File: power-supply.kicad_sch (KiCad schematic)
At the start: 16 parts, among them U1 LT3045EMSE_PBF_5.5V, U2 ADP150AUJZ-3.3-R7, U3 ADP150AUJZ-3.0-R7, U4 ADP150AUJZ-1.8-R7

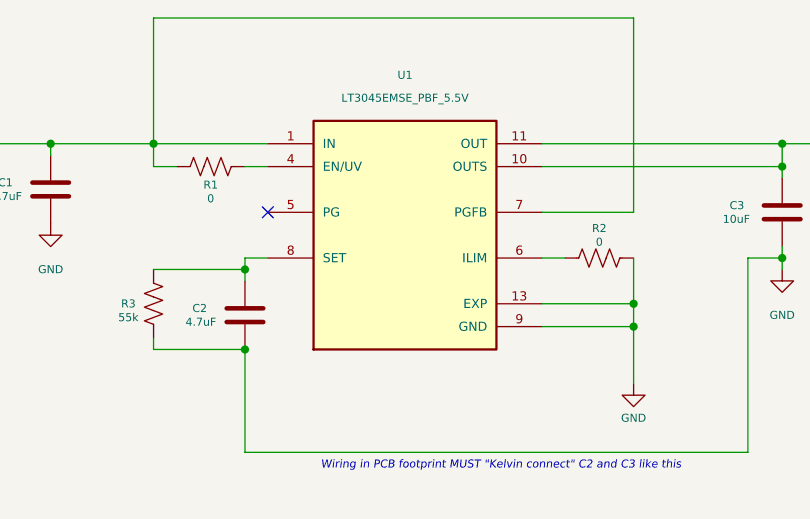
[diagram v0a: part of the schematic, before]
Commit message: Complete Schematic of the PCB
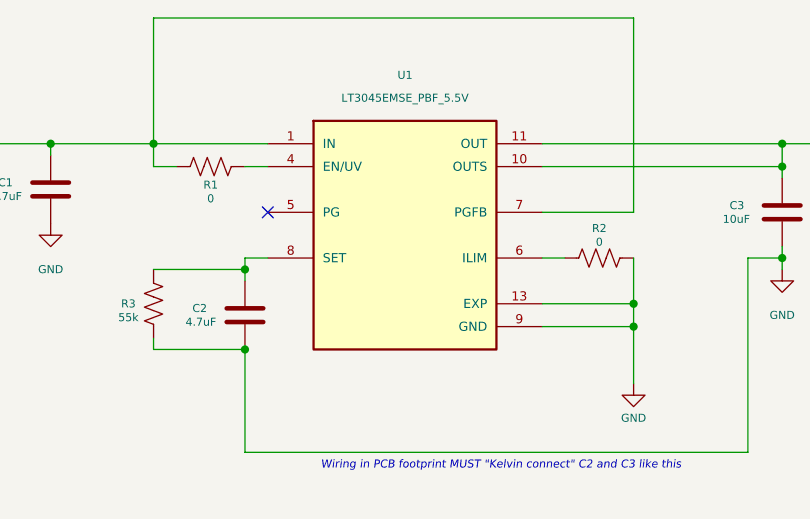
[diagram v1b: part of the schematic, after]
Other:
- title: Power Supply Module for the whole PLL system -> Power Supply Module for the PLL system
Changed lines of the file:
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@@
 	(paper "A4")
 	(title_block
-		(title "Power Supply Module for the whole PLL system")
+		(title "Power Supply Module for the PLL system")
 		(date "2026-08-31")
 		(rev "1")

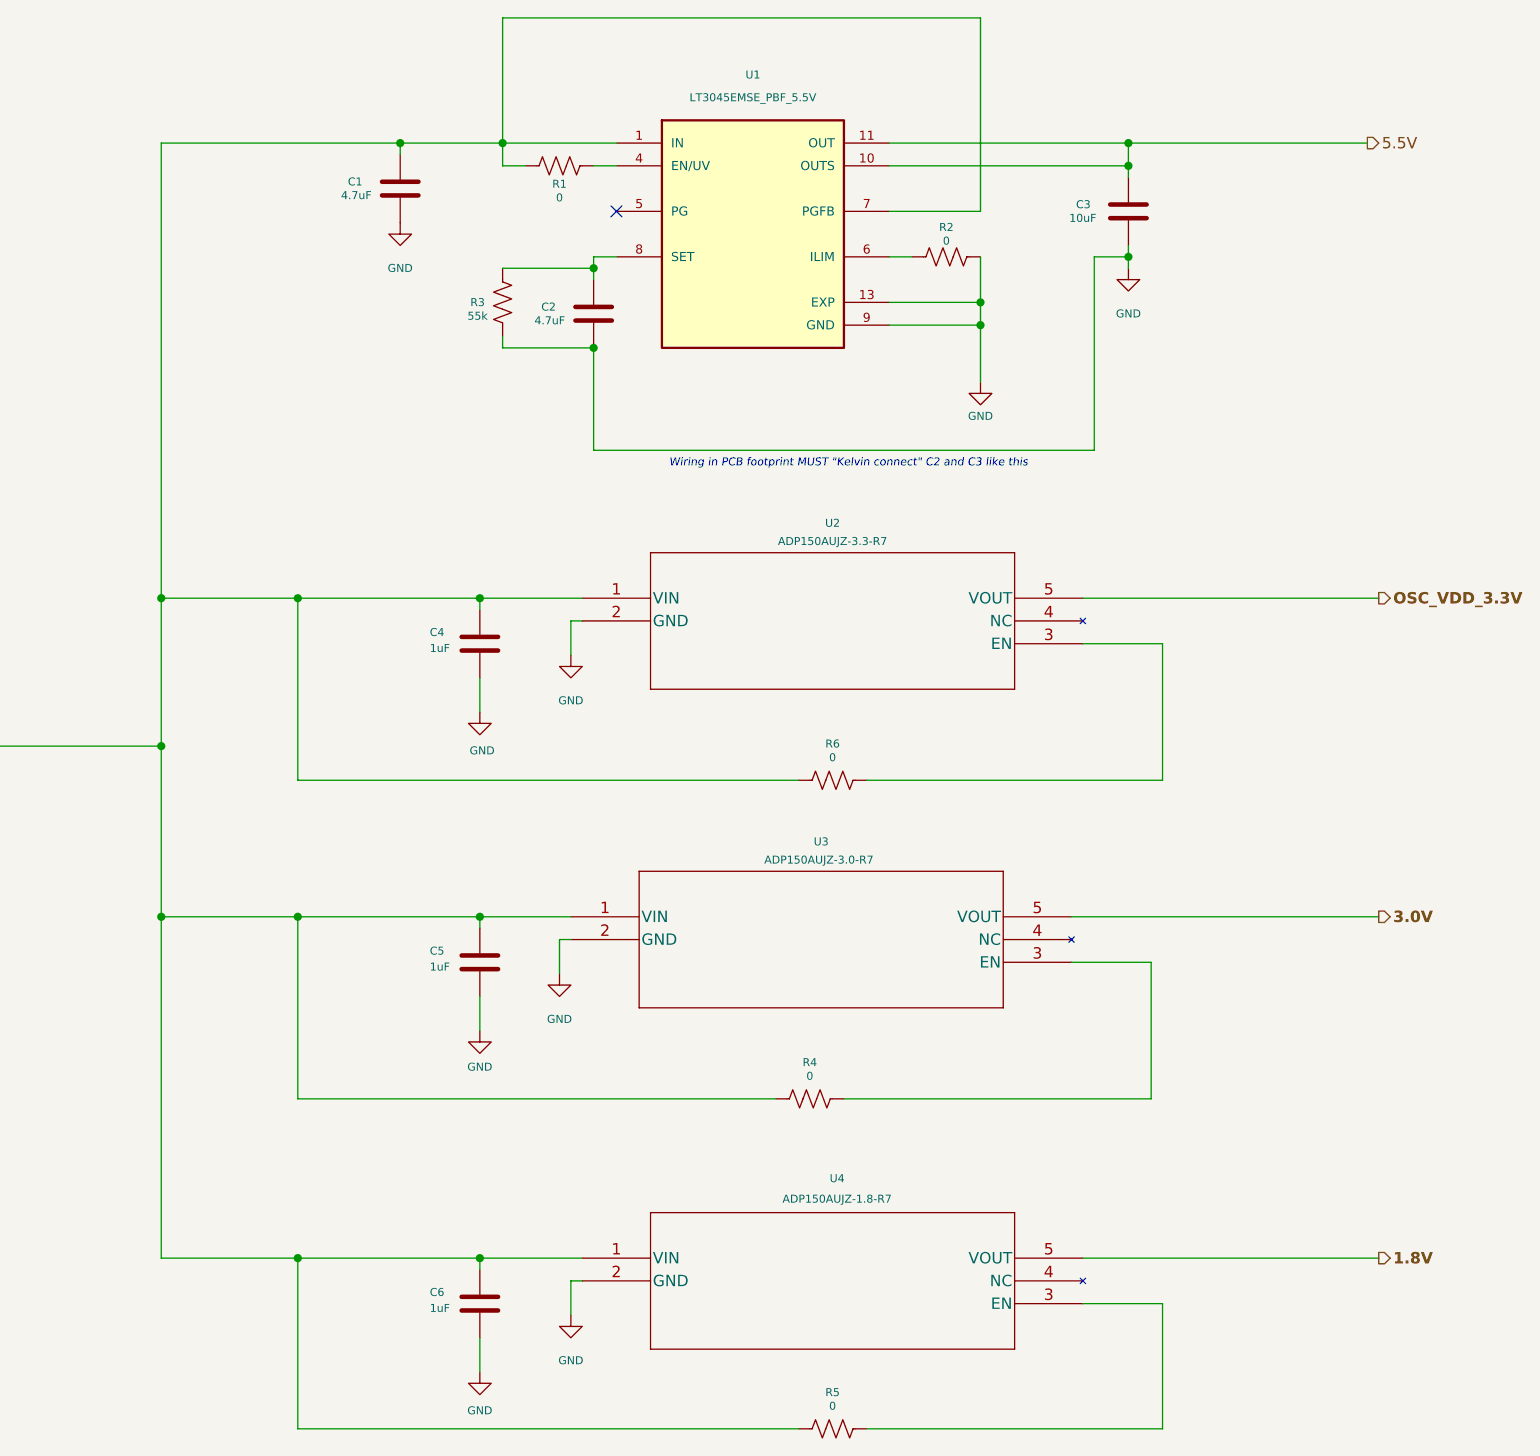
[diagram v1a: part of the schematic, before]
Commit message: Remove 0ohm resistors for EN pins and SMA connector for external REFIN
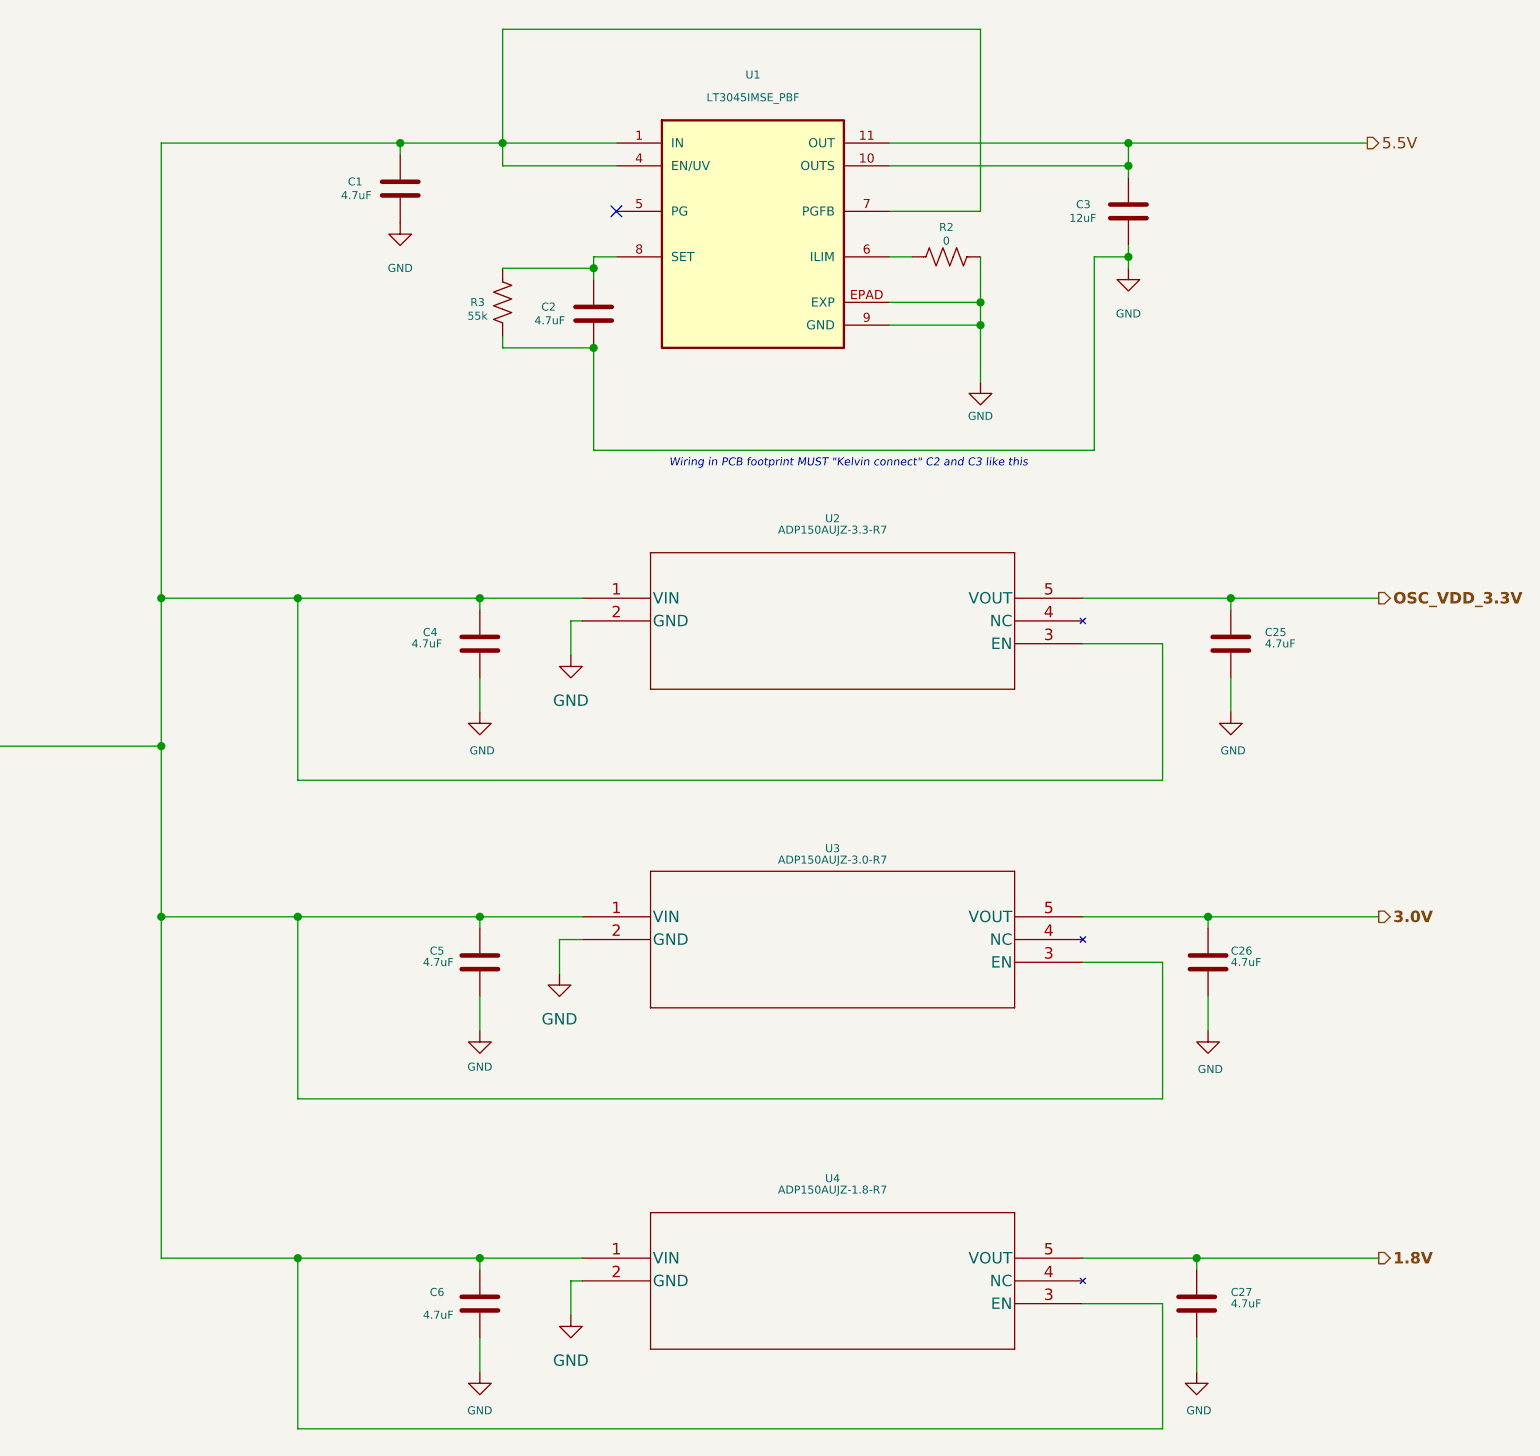
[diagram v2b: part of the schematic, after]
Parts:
- removed R1: 0, Capacitor_SMD:C_0603_1608Metric, symbol Device:R_US
- removed R4, R5, R6: 0, symbol Device:R_US
- removed U1: LT3045EMSE_PBF_5.5V, LT3045EMSE_PBF:SOP65P490X110-13N, symbol LT3045EMSE_PBF:LT3045EMSE_PBF
- removed U2: ADP150AUJZ-3.3-R7, ADP150AUJZ_3.3V_5_leads:UJ_5_ADI-M, symbol ADP150AUJZ_3.3V_5_leads:ADP150AUJZ-3.3-R7
- removed U3: ADP150AUJZ-3.0-R7, ADP150AUJZ_3.0V_5_leads:UJ_5_ADI-M, symbol ADP150AUJZ_5_leads:ADP150AUJZ-3.0-R7
- added C25, C26, C27: 4.7uF, Capacitor_SMD:C_0402_1005Metric, symbol Device:C
- added U1: LT3045IMSE_PBF, LT3045EMSE-5V5:MSOP12_MSE_ADI-L, symbol LT3045IMSE_PBF:LT3045IMSE_PBF
- added U2: ADP150AUJZ-3.3-R7, ADP150-3V3:UJ_5_ADI-L, symbol ADP150AUJZ_3.3_5_leads:ADP150AUJZ-3.3-R7
- added U3: ADP150AUJZ-3.0-R7, ADP150-3V:UJ_5_ADI-L, symbol ADP150AUJZ_3.0V_5_leads:ADP150AUJZ-3.0-R7
- C1, C2, R2, R3: footprint Capacitor_SMD:C_0603_1608Metric -> Capacitor_SMD:C_0402_1005Metric
- C3: value 10uF -> 12uF; footprint Capacitor_SMD:C_0603_1608Metric -> Capacitor_SMD:C_1206_3216Metric
- C4, C5, C6: value 1uF -> 4.7uF
- U4: footprint ADP150AUJZ_1.8V_5_leads:UJ_5_ADI-M -> ADP150-1V8:UJ_5_ADI-L
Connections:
- net +6.5V_RAW: now also U4.3 (EN), U1.1 (IN), U1.2 (IN), U1.3 (IN), U1.4 (EN/UV), U1.7 (PGFB), U2.1 (VIN), U2.3 (EN), U3.1 (VIN), U3.3 (EN)
- net 1.8V: now also C27.1
- net 3.0V: now also C26.1, U3.5 (VOUT)
- net 5.5V: now also U1.10 (OUTS), U1.11 (OUT), U1.12 (OUT)
- net GND: now also C25.2, C26.2, C27.2, U1.9 (GND), U1.EPAD (EXP), U2.2 (GND), U3.2 (GND)
- net OSC_VDD_3.3V: now also C25.1, U2.5 (VOUT)
- net at C2.1, R3.1: now also U1.8 (SET)
- net at R2.2: now also U1.6 (ILIM)

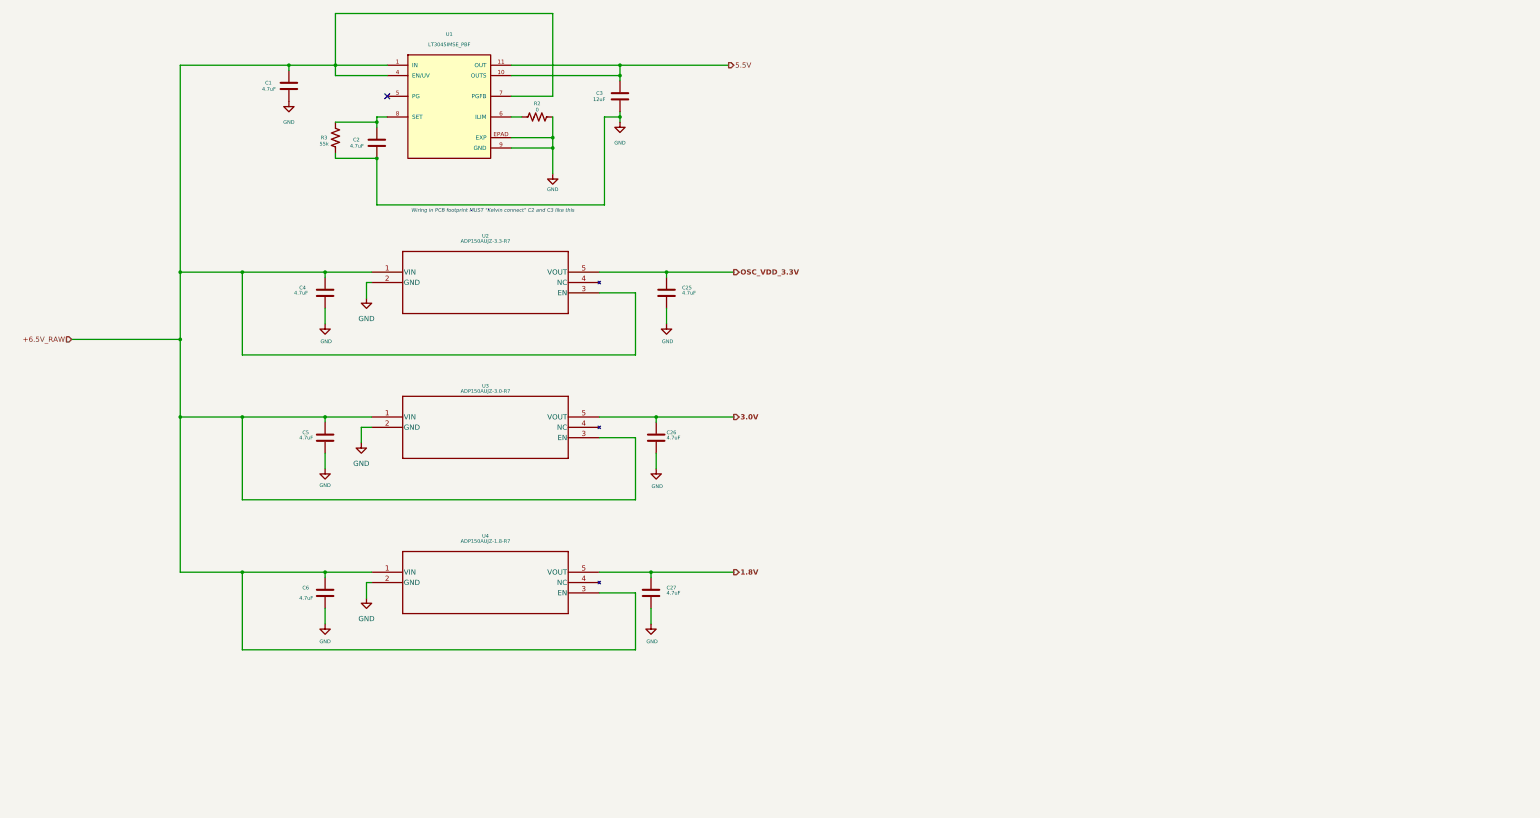
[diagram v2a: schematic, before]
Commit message: Complete and adjust the PCB based on advisor's advice and manufacturer in-stock parts
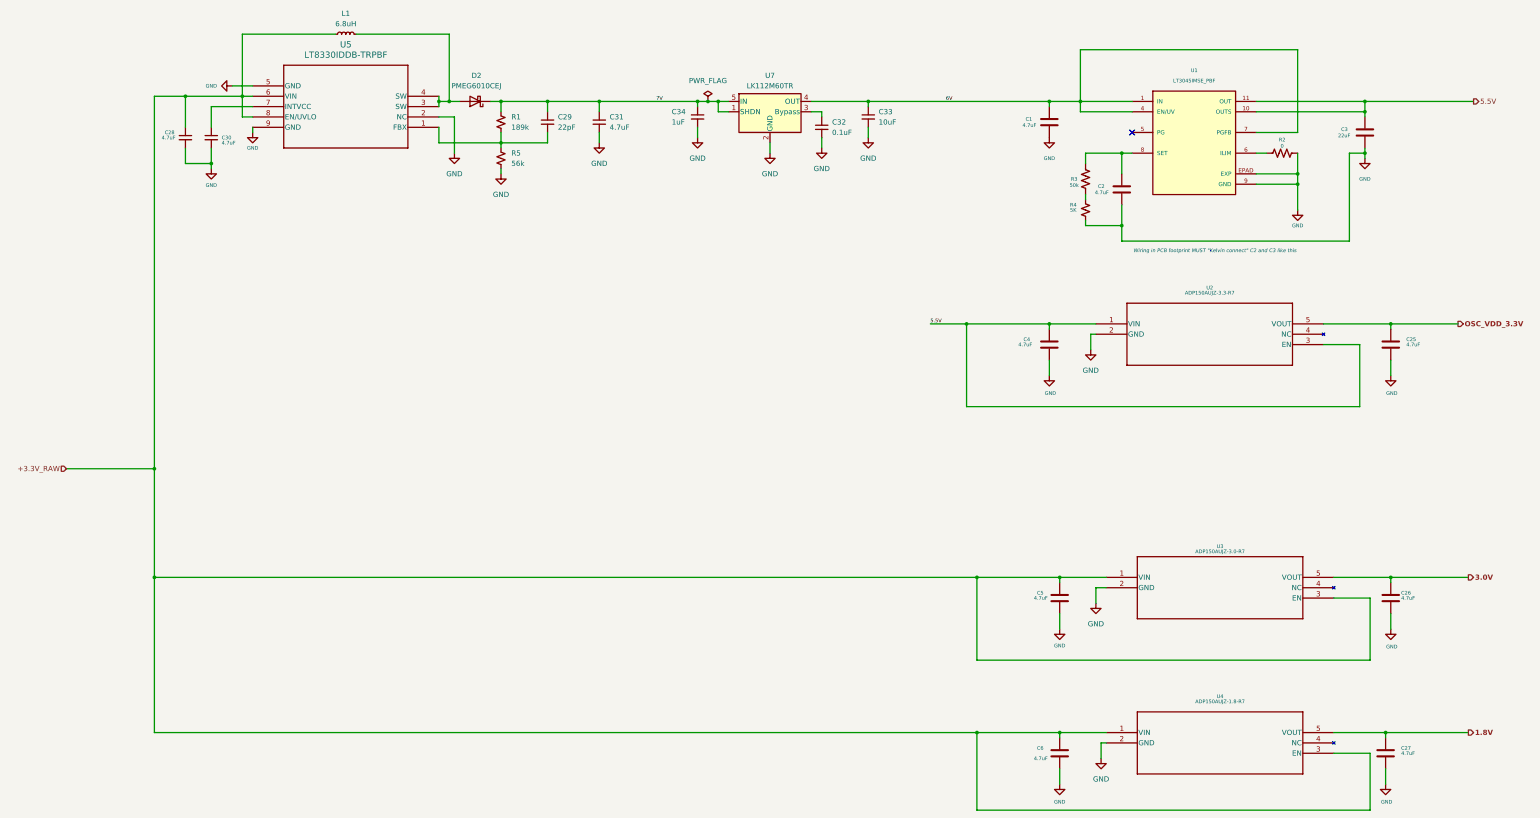
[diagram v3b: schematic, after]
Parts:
- added C28, C30, C31: 4.7uF, Capacitor_SMD:C_0402_1005Metric, symbol Device:C_Small
- added C29: 22pF, Capacitor_SMD:C_0402_1005Metric, symbol Device:C_Small
- added C32: 0.1uF, Capacitor_SMD:C_0402_1005Metric, symbol Device:C_Small
- added C33: 10uF, Capacitor_SMD:C_0603_1608Metric, symbol Device:C_Small
- added C34: 1uF, Capacitor_SMD:C_0402_1005Metric, symbol Device:C_Small
- added D2: PMEG6010CEJ, Diode_SMD:D_SOD-323F, symbol Diode:PMEG6010CEJ
- added L1: 6.8uH, Inductor_SMD:L_0603_1608Metric, symbol Device:L_Small
- added R1: 189k, Resistor_SMD:R_0603_1608Metric, symbol Device:R_Small_US
- added R4: 5K, Resistor_SMD:R_0402_1005Metric, symbol Device:R_Small_US
- added R5: 56k, Resistor_SMD:R_0805_2012Metric, symbol Device:R_Small_US
- added U5: LT8330IDDB-TRPBF, symbols:DDB_05-08-1702_ADI-L, symbol LT8330IDDB:LT8330IDDB-TRPBF
- added U7: LK112M60TR, Package_TO_SOT_SMD:SOT-23-5, symbol Regulator_Linear:LK112M60TR
- C3: value 12uF -> 22uF; footprint Capacitor_SMD:C_1206_3216Metric -> Capacitor_SMD:C_0603_1608Metric
- R2: footprint Capacitor_SMD:C_0402_1005Metric -> Resistor_SMD:R_0402_1005Metric
- R3: value 55k -> 50k; footprint Capacitor_SMD:C_0402_1005Metric -> Resistor_SMD:R_0402_1005Metric
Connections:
- net 5.5V: now also C4.1, U2.1 (VIN), U2.3 (EN)
- net GND: now also C28.2, C30.2, C31.2, C32.2, C33.2, C34.2, R4.2, R5.1, U5.2 (NC), U5.5 (GND), U5.9 (GND), U7.2 (GND); no longer R3.2
- removed net +6.5V_RAW: C1.1, C4.1, C5.1, C6.1, U1.1 (IN), U1.2 (IN), U1.3 (IN), U1.4 (EN/UV), U1.7 (PGFB), U2.1 (VIN), U2.3 (EN), U3.1 (VIN), U3.3 (EN), U4.1 (VIN), U4.3 (EN)
- new net: C29.2, R1.1, R5.2, U5.1 (FBX)
- new net: D2.2 (A), L1.2, U5.3 (SW), U5.4 (SW)
- new net: C30.1, U5.7 (INTVCC)
- new net: C32.1, U7.3 (Bypass)
- new net: R3.2, R4.1
- new net +3.3V_RAW: C28.1, C5.1, C6.1, L1.1, U3.1 (VIN), U3.3 (EN), U4.1 (VIN), U4.3 (EN), U5.6 (VIN), U5.8 (EN/UVLO)
- new net 6V: C1.1, C33.1, U1.1 (IN), U1.2 (IN), U1.3 (IN), U1.4 (EN/UV), U1.7 (PGFB), U7.4 (OUT)
- new net 7V: C29.1, C31.1, C34.1, D2.1 (K), R1.2, U7.1 (SHDN), U7.5 (IN)
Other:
- moved on the sheet: C1, C2, C25, C26, C27, C3, C4, C5, C6, R2, R3, U1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
